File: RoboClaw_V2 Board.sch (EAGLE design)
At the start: 11 parts

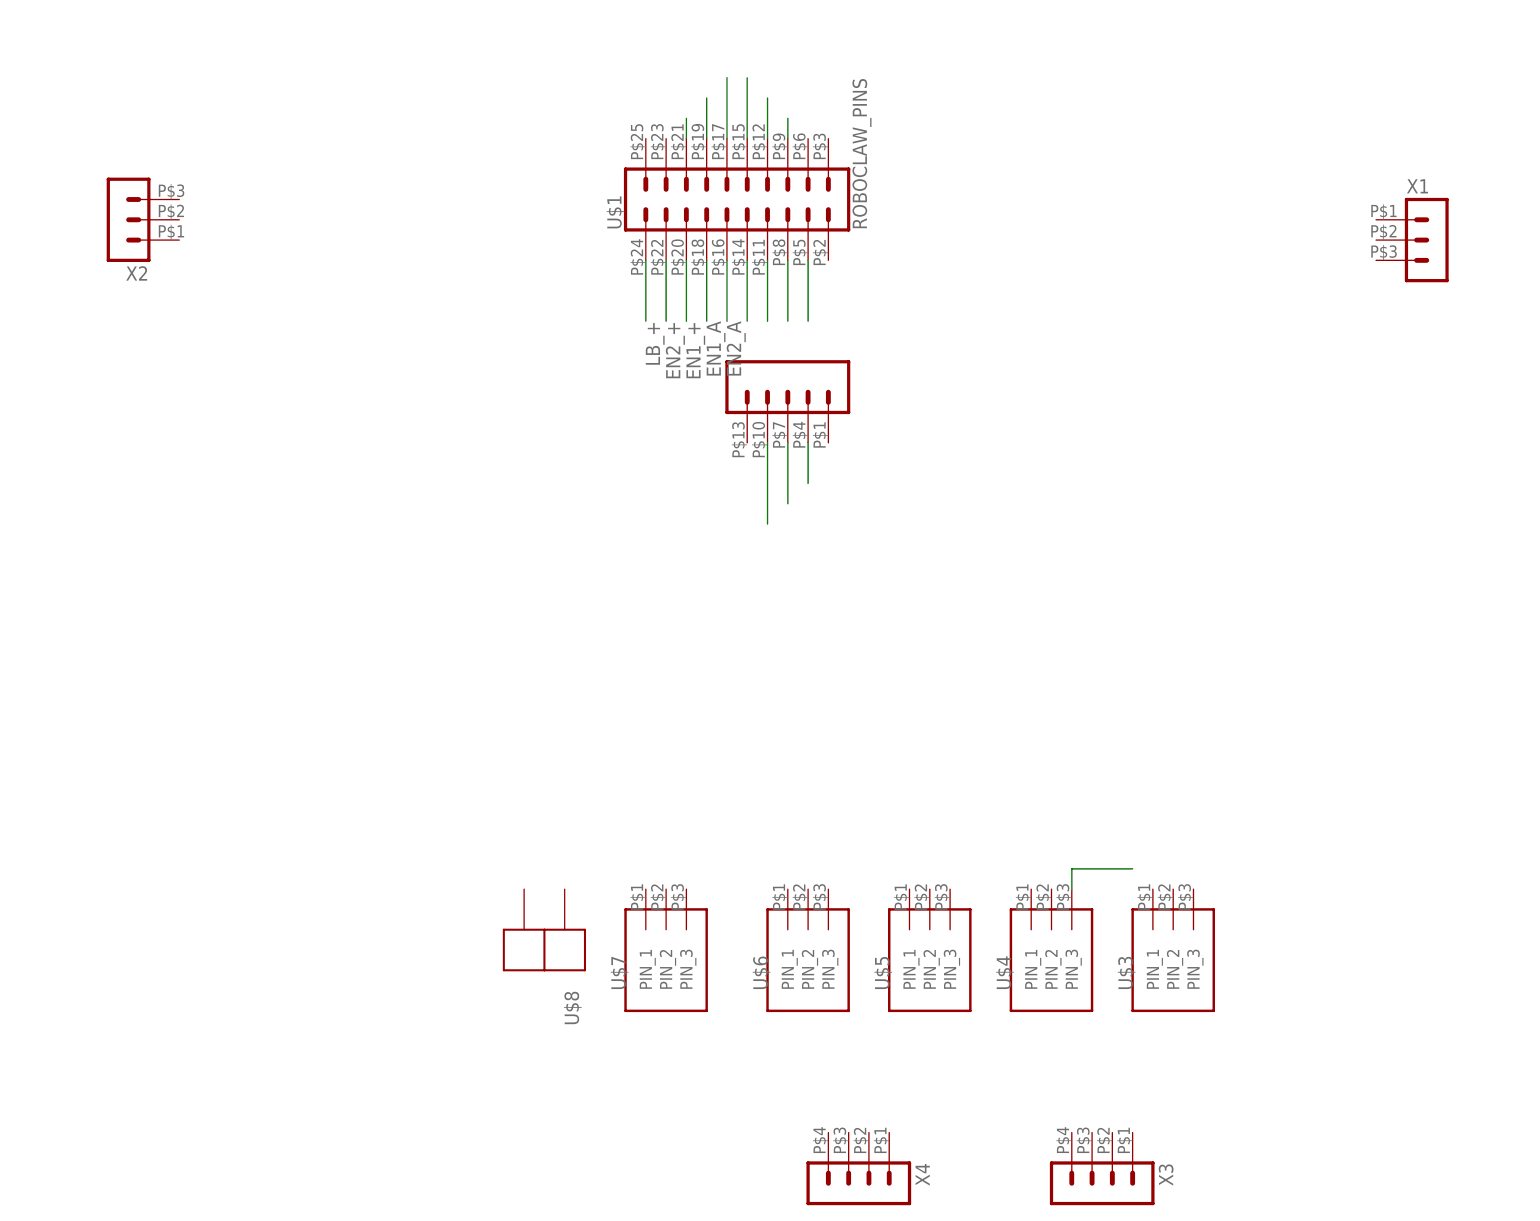
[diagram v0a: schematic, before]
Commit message: connected nets to encoders/serial lines/battery
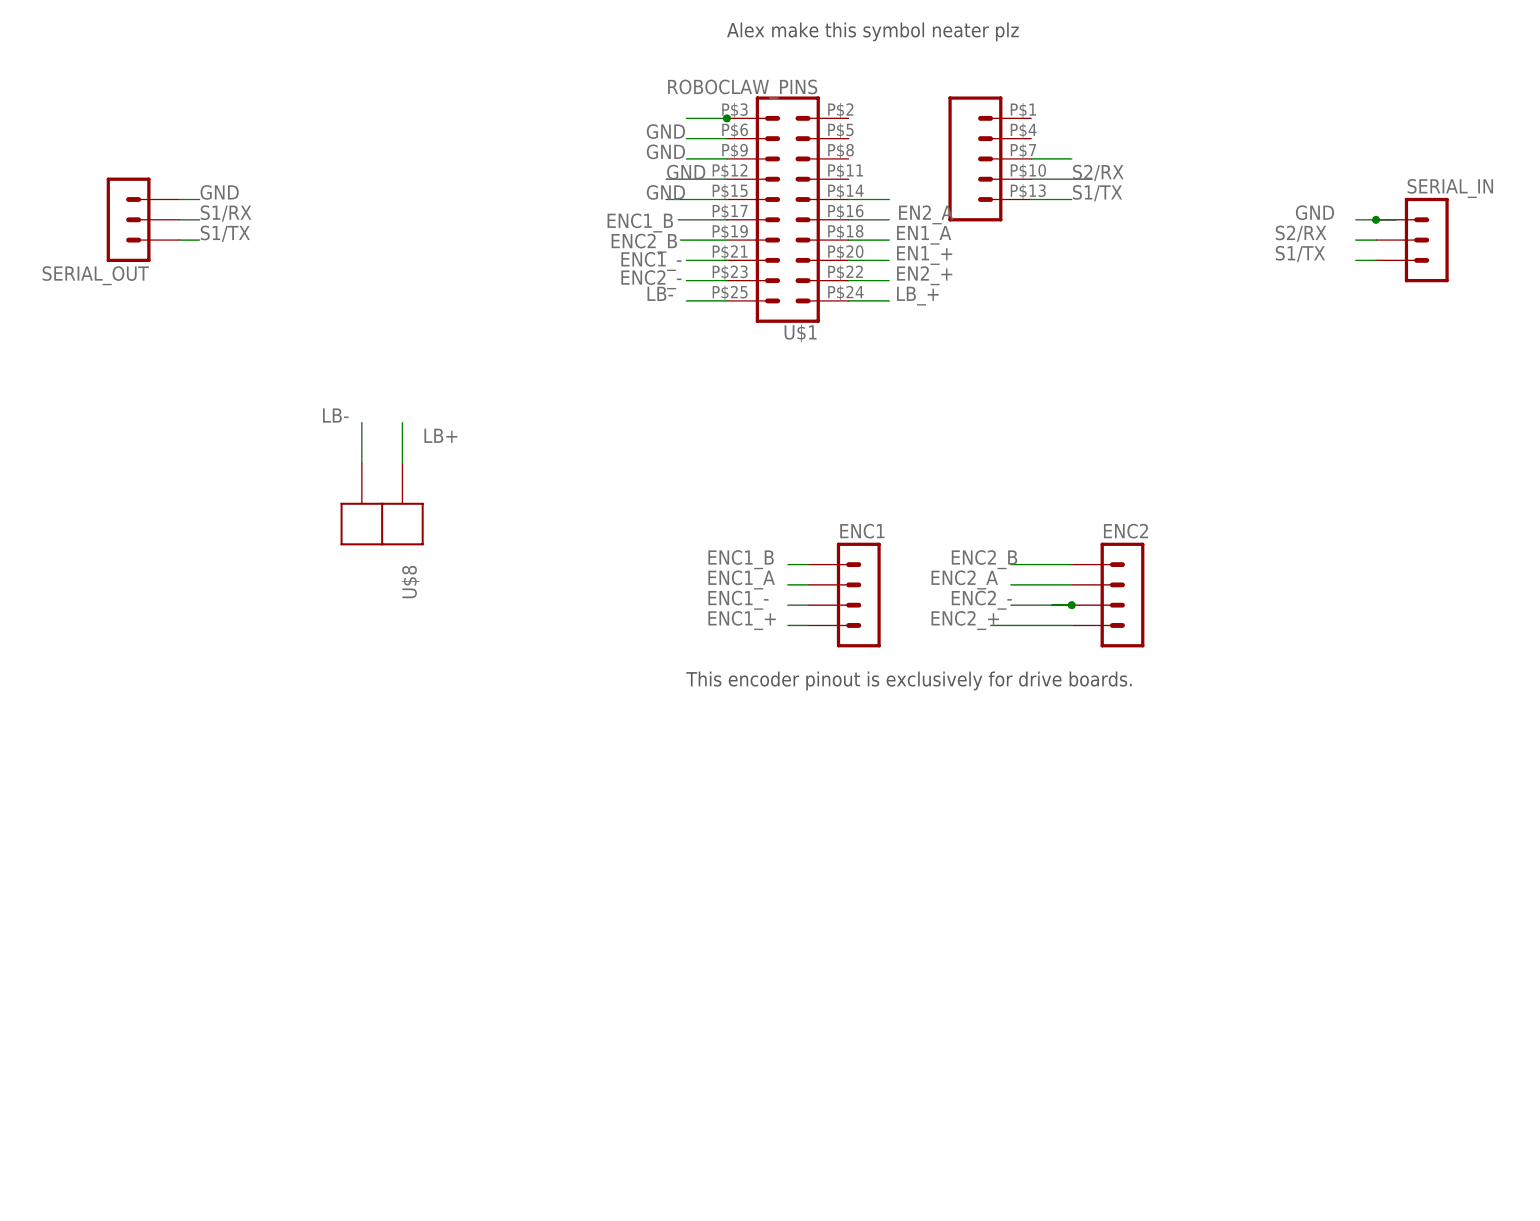
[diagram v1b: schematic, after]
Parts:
- removed U$3, U$4, U$5, U$6, U$7: (no value), Screw Blocks:3_PIN
- removed X3, X4: (no value), con-molex-micro-fit-3_0:HEADER_POS4_43045-0401
- added ENC1, ENC2: (no value), con-molex-micro-fit-3_0:HEADER_POS4_43045-0401
- renumbered X1 to SERIAL_IN, X2 to SERIAL_OUT
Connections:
- removed net N$1: U$1.PIN_17
- removed net N$11: U$1.PIN_5
- removed net N$12: U$1.PIN_4
- removed net N$2: U$1.PIN_19
- removed net N$29: U$1.PIN_12
- removed net N$3: U$1.PIN_21
- removed net N$30: U$1.PIN_11
- removed net N$31: U$1.PIN_10
- removed net N$32: U$1.PIN_15
- removed net N$6: U$4.PIN_3
- removed net N$7: U$1.PIN_9
- removed net N$8: U$1.PIN_8
- new net ENC1_+: ENC1.4
- new net ENC1_-: ENC1.3, U$1.PIN_21
- new net ENC1_A: ENC1.2
- new net ENC1_B: ENC1.1, U$1.PIN_17
- new net ENC2_+: ENC2.4
- new net ENC2_-: ENC2.3, U$1.PIN_23
- new net ENC2_A: ENC2.2
- new net ENC2_B: ENC2.1, U$1.PIN_19
- new net GND: SERIAL_IN.1, SERIAL_OUT.3, U$1.PIN_12, U$1.PIN_15, U$1.PIN_3, U$1.PIN_6, U$1.PIN_9
- new net LB+: U$8.P$1
- new net LB-: U$1.PIN_25, U$8.P$2
- new net S1/RX: SERIAL_OUT.2
- new net S1/TX: SERIAL_IN.3, SERIAL_OUT.1, U$1.PIN_13
- new net S2/RX: SERIAL_IN.2, U$1.PIN_10
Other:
- note added: "Alex make this symbol neater plz"
- note added: "This encoder pinout is exclusively for drive boards."
- moved on the sheet: U$1, U$8
